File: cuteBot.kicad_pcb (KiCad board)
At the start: 2 copper layers, 39.9 x 39.9 mm, 73 parts, among them P1 USB_A, P2 BAT+, P3 BAT-, P4 MOTOR_A, P5 MOTOR_B, P6 CONN_02X03, Q1 S8050, SW1 SW_SPDT, SW2 SW_Push, SW3 SW_Push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

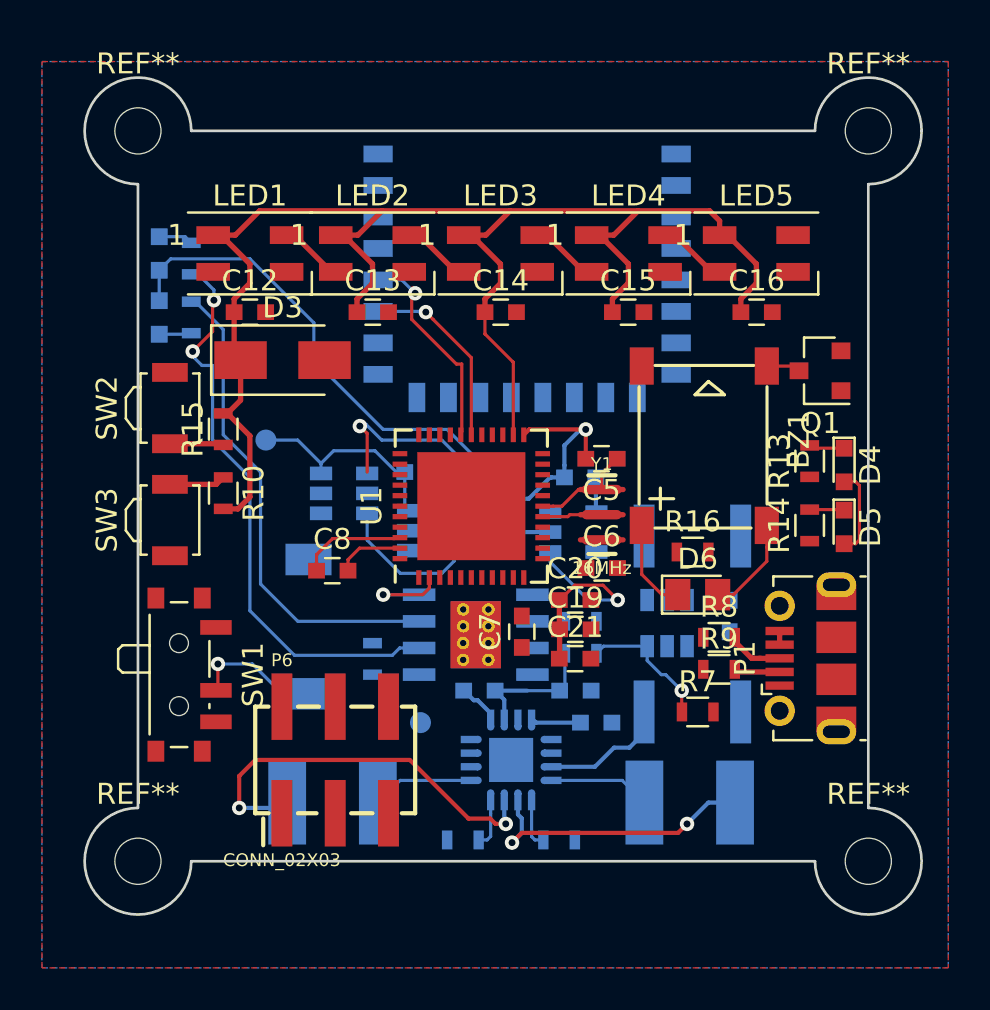
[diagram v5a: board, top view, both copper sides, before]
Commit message: Resonador cambiado
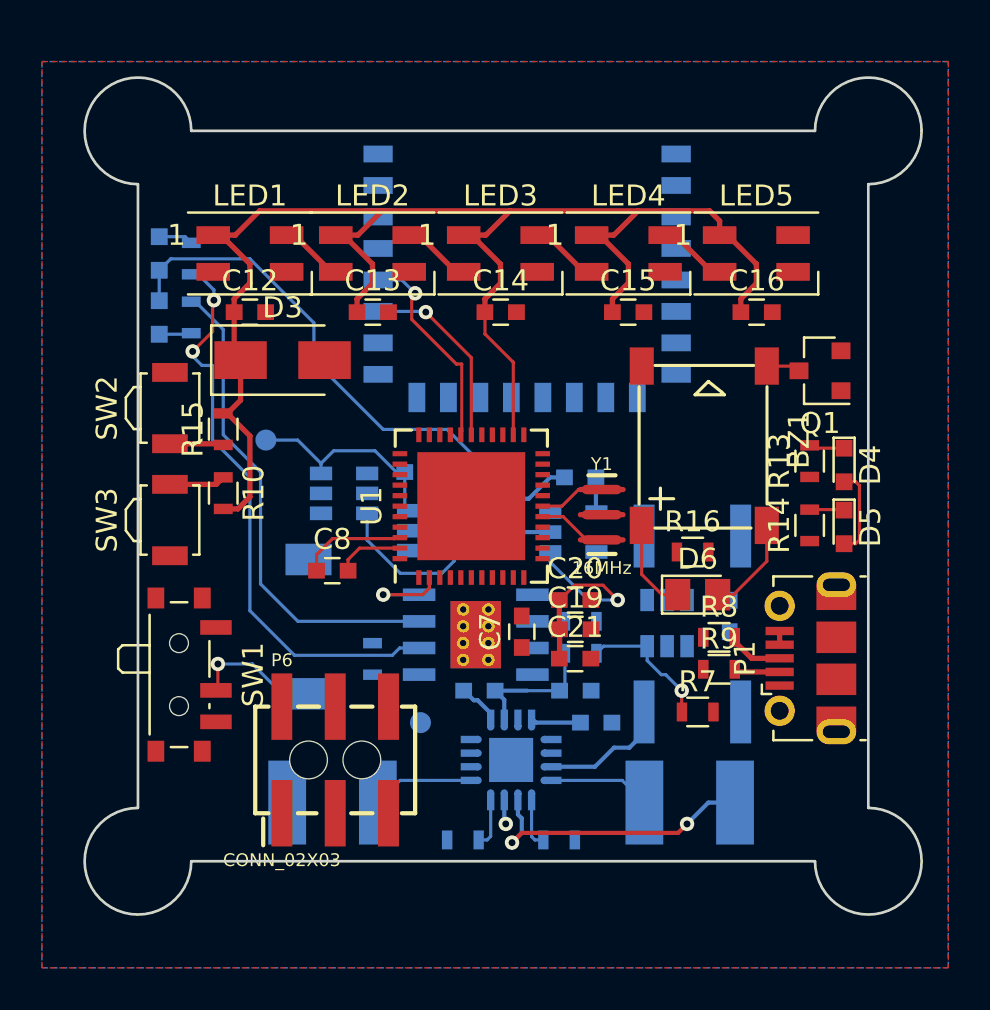
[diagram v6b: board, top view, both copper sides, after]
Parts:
- removed C5, C6: 22pF, Capacitors_SMD:C_0603
- removed REF** (x4): MountingHole_2.2mm_M2, Mounting_Holes:MountingHole_2.2mm_M2
- P6: footprint Connectors:2X3_SMT_POSTS_withoput_holes -> Connectors:2X3_SMT_POSTS
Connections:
- U1 pad 16: Net-(C6-Pad1) -> Net-(U1-Pad16)
- Y1 pad 2: Net-(C6-Pad1) -> GND
- Y1 pad 3: (no net) -> Net-(U1-Pad16)
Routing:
- net Net-(P5-Pad2): track 19.3 -> 1.45 mm, vias 2 -> 1
- net Net-(U3-Pad1): track 10.8 -> 0.00 mm, vias 1 -> 0
- net GND: track 15.5 -> 8.23 mm, vias 1 -> 0
- net Net-(U1-Pad16): track 0.00 -> 3.27 mm
- net Net-(C6-Pad1): track 2.85 -> 0.00 mm
- net Net-(U1-Pad17): track 4.93 -> 3.14 mm

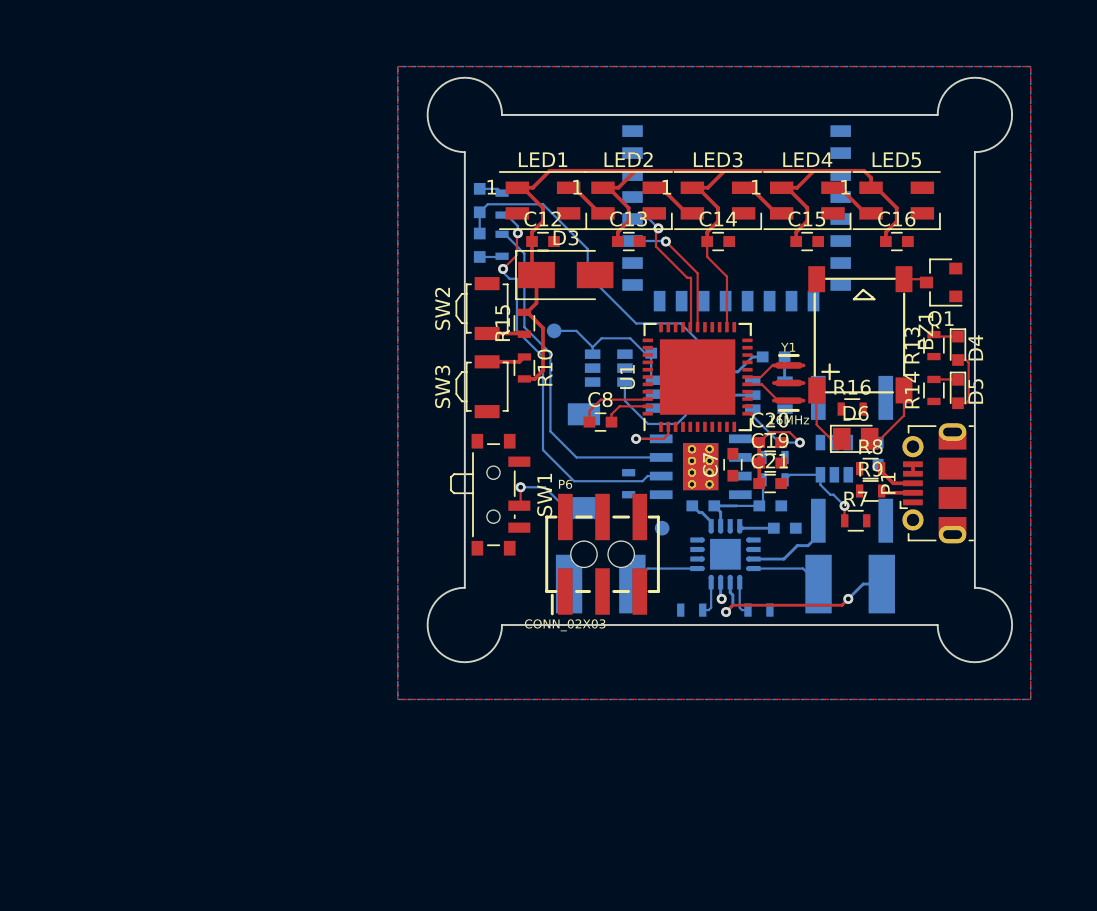
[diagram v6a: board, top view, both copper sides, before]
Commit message: Leds RX/TX eliminados
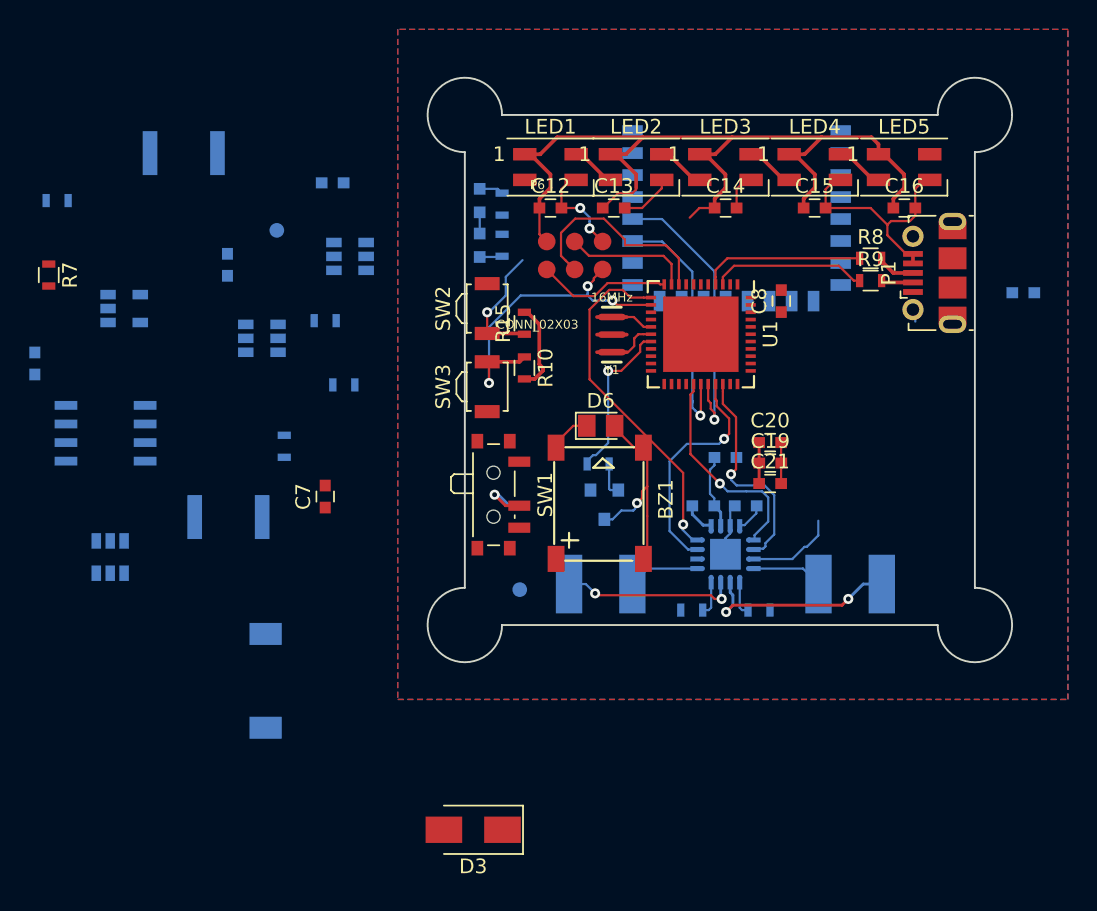
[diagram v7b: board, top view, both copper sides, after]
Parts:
- removed D4: GREEN, LEDs:LED_0603
- removed D5: RED, LEDs:LED_0603
- removed R13, R14: 330, Resistors_SMD:R_0603
- Q1, R16: moved to B.Cu
- moved C18 57.9 mm to (92.1, 134.6)
- moved R7 57.6 mm to (93.0, 128.5), turned to 270 degrees
- moved R1 52.0 mm to (93.6, 123.4)
- moved U5 49.9 mm to (97.2, 147.8)
- moved C3 48.6 mm to (102.2, 120.2)
- moved U8 44.4 mm to (98.2, 130.8)
- moved C4 42.5 mm to (105.3, 145.0)
- moved U2 40.7 mm to (96.9, 139.3)
- moved D3 38.4 mm to (122.0, 166.4), turned to 180 degrees
- moved C17 37.8 mm to (105.2, 127.8), turned to 270 degrees
- moved R6 30.1 mm to (113.2, 136.0)
- moved U3 28.1 mm to (107.6, 132.8)
- moved C7 27.9 mm to (111.9, 143.6)
- moved Q1 27.5 mm to (130.9, 144.2), turned to 270 degrees
- moved R5 27.3 mm to (111.9, 131.6)
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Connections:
- U1 pad 22: TX_LED -> Net-(U1-Pad22)
- U1 pad 8: RX_LED -> Net-(U1-Pad8)
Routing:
- net Net-(R2-Pad1): track 27.6 -> 0.00 mm, vias 2 -> 0
- net GND: track 8.23 -> 35.5 mm, vias 0 -> 2
- net Vusb: track 28.4 -> 1.45 mm, vias 1 -> 0
- net MOTOR_B_2: track 0.00 -> 23.9 mm, vias 0 -> 1
- net Net-(R3-Pad1): track 23.2 -> 0.00 mm
- net RST: track 2.68 -> 22.5 mm, vias 0 -> 3
- net 5V: track 103.2 -> 83.9 mm, vias 1 -> 0
- net MOTOR_B_1: track 0.00 -> 15.7 mm, vias 0 -> 1
- net MOTOR_A_1: track 0.00 -> 15.0 mm, vias 0 -> 1
- net MOTOR_A_2: track 0.00 -> 14.7 mm, vias 0 -> 1
- net SCK: track 0.00 -> 14.5 mm
- net Net-(R8-Pad1): track 0.00 -> 11.1 mm
- net BUZZ: track 0.00 -> 11.1 mm, vias 0 -> 1
- net Net-(P5-Pad2): track 1.45 -> 12.3 mm, vias 1 -> 2
- net Net-(R9-Pad1): track 0.00 -> 10.6 mm
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
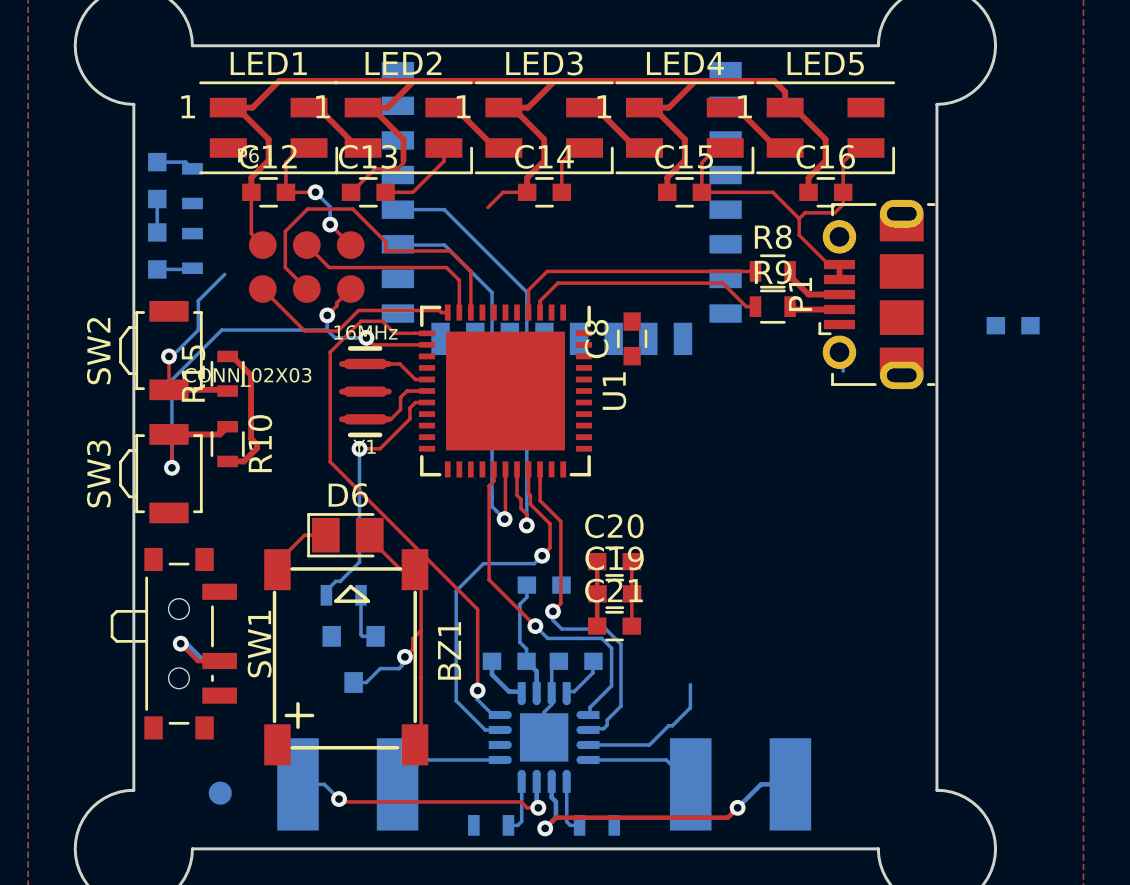
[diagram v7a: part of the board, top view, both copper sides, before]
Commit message: Enrutado avanzando. 65 nets
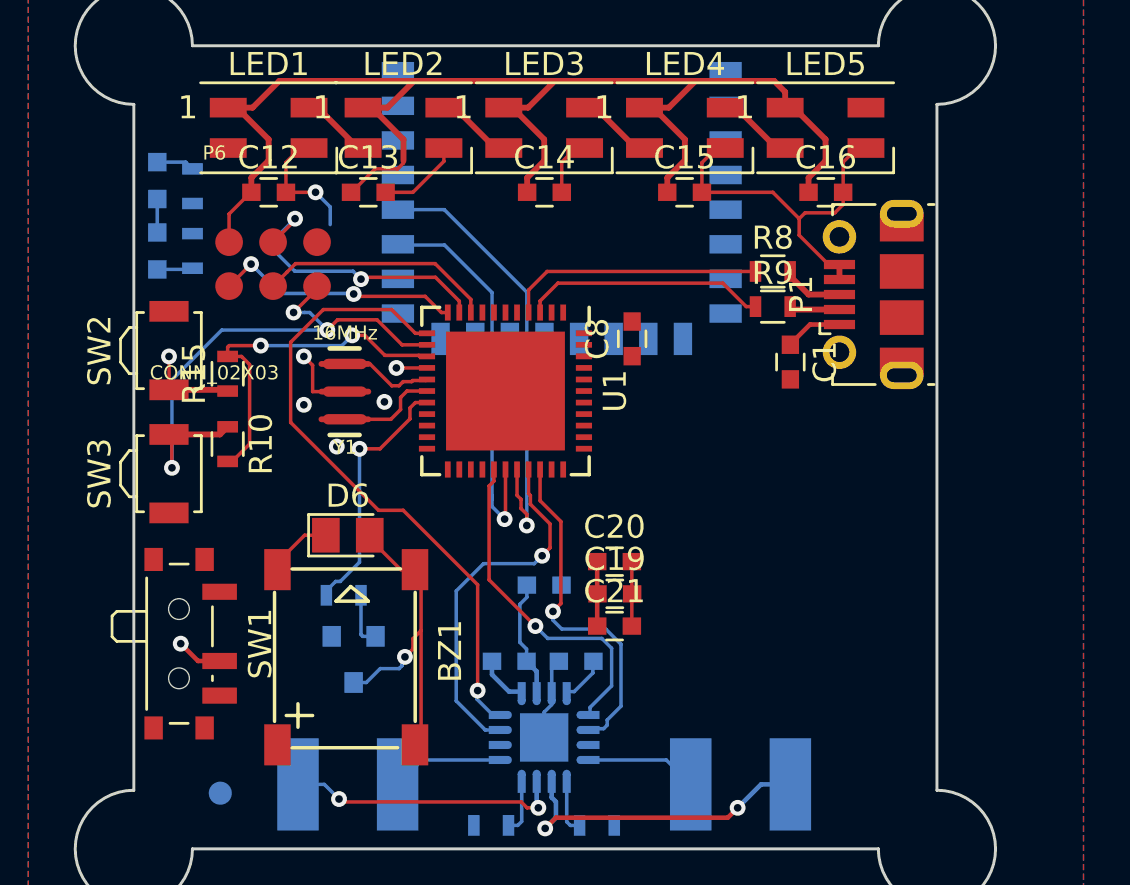
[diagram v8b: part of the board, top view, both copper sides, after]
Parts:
- C1: moved to F.Cu
- moved C1 9.78 mm to (149.9, 131.3), turned to 270 degrees
- moved P6 1.47 mm to (127.4, 127.0)
- moved Y1 0.89 mm to (130.6, 132.6)
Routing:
- net B1: track 8.64 -> 4.14 mm
- net SCK: track 14.5 -> 10.2 mm
- net MOSI: track 8.64 -> 12.8 mm, vias 0 -> 2
- net MOTOR_B_2: track 23.9 -> 27.6 mm
- net GND: track 35.5 -> 38.6 mm, vias 2 -> 6
- net Vusb: track 1.45 -> 3.95 mm
- net MISO: track 9.17 -> 10.7 mm, vias 0 -> 2
- net RST: track 22.5 -> 23.9 mm
- net 5V: track 83.9 -> 85.3 mm, vias 0 -> 2
- net Net-(C3-Pad1): track 3.54 -> 2.25 mm
